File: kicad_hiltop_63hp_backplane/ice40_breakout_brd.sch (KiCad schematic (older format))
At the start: 21 parts, among them J9 SO-DIMM

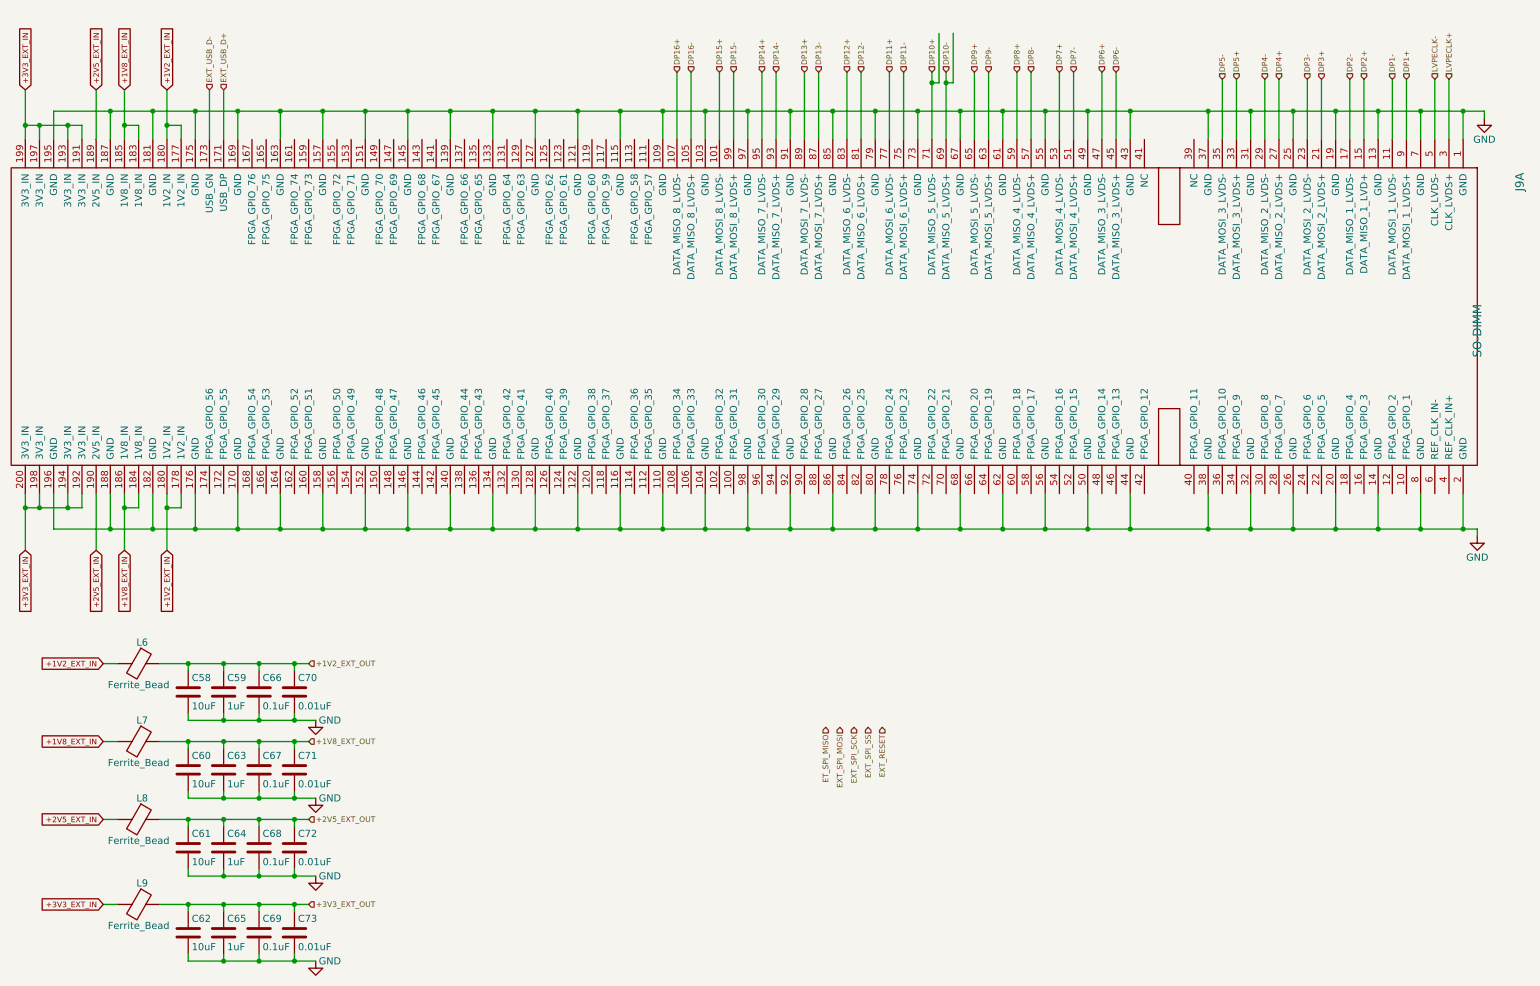
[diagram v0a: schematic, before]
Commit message: root - added pins for SODIMM, added PCI 96 pin connector, pin mapping in progress
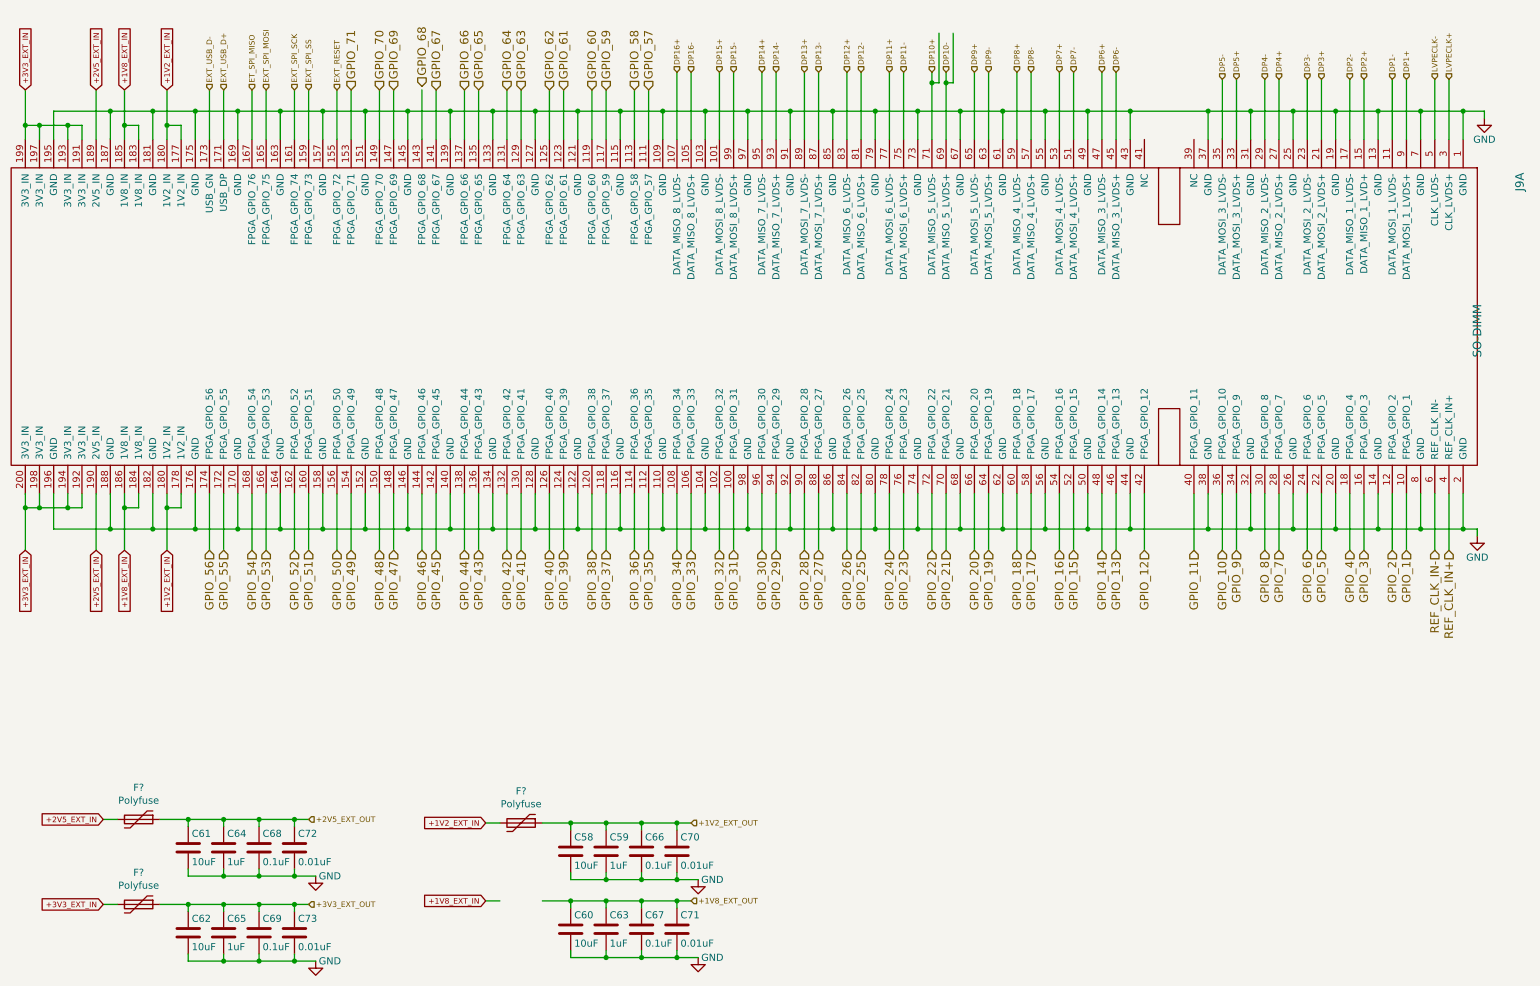
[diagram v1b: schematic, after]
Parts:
- removed L6, L7, L8, L9: Ferrite_Bead, Inductor_SMD:L_0603_1608Metric, symbol device:Ferrite_Bead
- added F? (x3): Polyfuse, symbol device:Polyfuse
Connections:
- net +1V2_EXT_IN: now also F?.2
- net +1V2_EXT_OUT: now also F?.1
- net +2V5_EXT_IN: now also F?.2
- net +2V5_EXT_OUT: now also F?.1
- net +3V3_EXT_IN: now also F?.2
- net +3V3_EXT_OUT: now also F?.1
- net ET_SPI_MISO: now also J9.167 (FPGA_GPIO_76)
- net EXT_RESET: now also J9.155 (FPGA_GPIO_72)
- net EXT_SPI_MOSI: now also J9.165 (FPGA_GPIO_75)
- net EXT_SPI_SCK: now also J9.161 (FPGA_GPIO_74)
- net EXT_SPI_SS: now also J9.159 (FPGA_GPIO_73)
- net GPIO_1: now reaches J9.10 (FPGA_GPIO_1)
- net GPIO_31: now reaches J9.100 (FPGA_GPIO_31)
- net GPIO_32: now reaches J9.102 (FPGA_GPIO_32)
- net GPIO_33: now reaches J9.106 (FPGA_GPIO_33)
- net GPIO_34: now reaches J9.108 (FPGA_GPIO_34)
- net GPIO_57: now reaches J9.111 (FPGA_GPIO_57)
- net GPIO_35: now reaches J9.112 (FPGA_GPIO_35)
- net GPIO_58: now reaches J9.113 (FPGA_GPIO_58)
- net GPIO_36: now reaches J9.114 (FPGA_GPIO_36)
- net GPIO_59: now reaches J9.117 (FPGA_GPIO_59)
- net GPIO_37: now reaches J9.118 (FPGA_GPIO_37)
- net GPIO_60: now reaches J9.119 (FPGA_GPIO_60)
- net GPIO_2: now reaches J9.12 (FPGA_GPIO_2)
- net GPIO_38: now reaches J9.120 (FPGA_GPIO_38)
- net GPIO_61: now reaches J9.123 (FPGA_GPIO_61)
- net GPIO_39: now reaches J9.124 (FPGA_GPIO_39)
- net GPIO_62: now reaches J9.125 (FPGA_GPIO_62)
- net GPIO_40: now reaches J9.126 (FPGA_GPIO_40)
- net GPIO_63: now reaches J9.129 (FPGA_GPIO_63)
- net GPIO_41: now reaches J9.130 (FPGA_GPIO_41)
- net GPIO_64: now reaches J9.131 (FPGA_GPIO_64)
- net GPIO_42: now reaches J9.132 (FPGA_GPIO_42)
- net GPIO_65: now reaches J9.135 (FPGA_GPIO_65)
- net GPIO_43: now reaches J9.136 (FPGA_GPIO_43)
- net GPIO_66: now reaches J9.137 (FPGA_GPIO_66)
- net GPIO_44: now reaches J9.138 (FPGA_GPIO_44)
- net GPIO_67: now reaches J9.141 (FPGA_GPIO_67)
- net GPIO_45: now reaches J9.142 (FPGA_GPIO_45)
- net GPIO_46: now reaches J9.144 (FPGA_GPIO_46)
- net GPIO_69: now reaches J9.147 (FPGA_GPIO_69)
- net GPIO_47: now reaches J9.148 (FPGA_GPIO_47)
- net GPIO_70: now reaches J9.149 (FPGA_GPIO_70)
- net GPIO_48: now reaches J9.150 (FPGA_GPIO_48)
- net GPIO_71: now reaches J9.153 (FPGA_GPIO_71)
- net GPIO_49: now reaches J9.154 (FPGA_GPIO_49)
- net GPIO_50: now reaches J9.156 (FPGA_GPIO_50)
- net GPIO_3: now reaches J9.16 (FPGA_GPIO_3)
- net GPIO_51: now reaches J9.160 (FPGA_GPIO_51)
- net GPIO_52: now reaches J9.162 (FPGA_GPIO_52)
- net GPIO_53: now reaches J9.166 (FPGA_GPIO_53)
- net GPIO_54: now reaches J9.168 (FPGA_GPIO_54)
- net GPIO_55: now reaches J9.172 (FPGA_GPIO_55)
- net GPIO_56: now reaches J9.174 (FPGA_GPIO_56)
- net GPIO_4: now reaches J9.18 (FPGA_GPIO_4)
- net GPIO_5: now reaches J9.22 (FPGA_GPIO_5)
- net GPIO_6: now reaches J9.24 (FPGA_GPIO_6)
- net GPIO_7: now reaches J9.28 (FPGA_GPIO_7)
- net GPIO_8: now reaches J9.30 (FPGA_GPIO_8)
- net GPIO_9: now reaches J9.34 (FPGA_GPIO_9)
- net GPIO_10: now reaches J9.36 (FPGA_GPIO_10)
- net REF_CLK_IN+: now reaches J9.4 (REF_CLK_IN+)
- net GPIO_11: now reaches J9.40 (FPGA_GPIO_11)
- net GPIO_12: now reaches J9.42 (FPGA_GPIO_12)
- net GPIO_13: now reaches J9.46 (FPGA_GPIO_13)
- net GPIO_14: now reaches J9.48 (FPGA_GPIO_14)
- net GPIO_15: now reaches J9.52 (FPGA_GPIO_15)
- net GPIO_16: now reaches J9.54 (FPGA_GPIO_16)
- net GPIO_17: now reaches J9.58 (FPGA_GPIO_17)
- net REF_CLK_IN-: now reaches J9.6 (REF_CLK_IN-)
- net GPIO_18: now reaches J9.60 (FPGA_GPIO_18)
- net GPIO_19: now reaches J9.64 (FPGA_GPIO_19)
- net GPIO_20: now reaches J9.66 (FPGA_GPIO_20)
- net GPIO_21: now reaches J9.70 (FPGA_GPIO_21)
- net GPIO_22: now reaches J9.72 (FPGA_GPIO_22)
- net GPIO_23: now reaches J9.76 (FPGA_GPIO_23)
- net GPIO_24: now reaches J9.78 (FPGA_GPIO_24)
- net GPIO_25: now reaches J9.82 (FPGA_GPIO_25)
- net GPIO_26: now reaches J9.84 (FPGA_GPIO_26)
- net GPIO_27: now reaches J9.88 (FPGA_GPIO_27)
- net GPIO_28: now reaches J9.90 (FPGA_GPIO_28)
- net GPIO_29: now reaches J9.94 (FPGA_GPIO_29)
- net GPIO_30: now reaches J9.96 (FPGA_GPIO_30)
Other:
- moved on the sheet: C58, C59, C60, C63, C66, C67, C70, C71

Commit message: PCI EXPRESS 96
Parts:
- gave numbers to parts that had none: 3
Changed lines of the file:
@@
 GPIO_71
 $Comp
-L device:Polyfuse F?
+L device:Polyfuse F9
 U 1 1 5CEC5F97
 P 1600 6500
-F 0 "F?" V 1375 6500 50  0000 C CNN
+F 0 "F9" V 1375 6500 50  0000 C CNN
 F 1 "Polyfuse" V 1466 6500 50  0000 C CNN
 F 2 "" H 1650 6300 50  0001 L CNN
@@
 $EndComp
 $Comp
-L device:Polyfuse F?
+L device:Polyfuse F10
 U 1 1 5CEC61F6
 P 1600 7100
-F 0 "F?" V 1375 7100 50  0000 C CNN
+F 0 "F10" V 1375 7100 50  0000 C CNN
 F 1 "Polyfuse" V 1466 7100 50  0000 C CNN
 F 2 "" H 1650 6900 50  0001 L CNN
@@
 $EndComp
 $Comp
-L device:Polyfuse F?
+L device:Polyfuse F11
 U 1 1 5CEC625C
 P 4300 6525
-F 0 "F?" V 4075 6525 50  0000 C CNN
+F 0 "F11" V 4075 6525 50  0000 C CNN
 F 1 "Polyfuse" V 4166 6525 50  0000 C CNN
 F 2 "" H 4350 6325 50  0001 L CNN

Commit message: Added new PCB outline for the backplane
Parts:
- C58, C59, C60, C61, C62, C63, C64, C65, C66, C67, C68, C69, C70, C71, C72, C73: symbol device:C -> hiltop_backplane_brd-rescue:C-device
- F10, F11, F9: symbol device:Polyfuse -> hiltop_backplane_brd-rescue:Polyfuse-device
- J9: symbol gti_Lattice:SO-DIMM -> hiltop_backplane_brd-rescue:SO-DIMM-gti_Lattice
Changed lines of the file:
@@
 $EndDescr
 $Comp
-L device:C C58
+L hiltop_backplane_brd-rescue:C-device C58
 U 1 1 5A418459
 P 4650 6725
@@
 $EndComp
 $Comp
-L device:C C59
+L hiltop_backplane_brd-rescue:C-device C59
 U 1 1 5A4184EA
 P 4900 6725
@@
 $EndComp
 $Comp
-L device:C C66
+L hiltop_backplane_brd-rescue:C-device C66
 U 1 1 5A41850F
 P 5150 6725
@@
 $EndComp
 $Comp
-L device:C C70
+L hiltop_backplane_brd-rescue:C-device C70
 U 1 1 5A418541
 P 5400 6725
@@
 $EndComp
 $Comp
-L device:C C60
+L hiltop_backplane_brd-rescue:C-device C60
 U 1 1 5A41856A
 P 4650 7275
@@
 $EndComp
 $Comp
-L device:C C63
+L hiltop_backplane_brd-rescue:C-device C63
 U 1 1 5A4185BC
 P 4900 7275
@@
 $EndComp
 $Comp
-L device:C C67
+L hiltop_backplane_brd-rescue:C-device C67
 U 1 1 5A4185F9
 P 5150 7275
@@
 $EndComp
 $Comp
-L device:C C71
+L hiltop_backplane_brd-rescue:C-device C71
 U 1 1 5A41862F
 P 5400 7275
@@
 $EndComp
 $Comp
-L device:C C61
+L hiltop_backplane_brd-rescue:C-device C61
 U 1 1 5A418664
 P 1950 6700
@@
 $EndComp
 $Comp
-L device:C C64
+L hiltop_backplane_brd-rescue:C-device C64
 U 1 1 5A4186B2
 P 2200 6700
@@
 $EndComp
 $Comp
-L device:C C68
+L hiltop_backplane_brd-rescue:C-device C68
 U 1 1 5A4186E9
 P 2450 6700
@@
 $EndComp
 $Comp
-L device:C C72
+L hiltop_backplane_brd-rescue:C-device C72
 U 1 1 5A418729
 P 2700 6700
@@
 $EndComp
 $Comp
-L device:C C62
+L hiltop_backplane_brd-rescue:C-device C62
 U 1 1 5A418776
 P 1950 7300
@@
 $EndComp
 $Comp
-L device:C C65
+L hiltop_backplane_brd-rescue:C-device C65
 U 1 1 5A418B7E
 P 2200 7300
@@
 $EndComp
 $Comp
-L device:C C69
+L hiltop_backplane_brd-rescue:C-device C69
 U 1 1 5A418BC9
 P 2450 7300
@@
 $EndComp
 $Comp
-L device:C C73
+L hiltop_backplane_brd-rescue:C-device C73
 U 1 1 5A418C13
 P 2700 7300
@@
 	8600 1500 9150 1500
 $Comp
-L gti_Lattice:SO-DIMM J9
+L hiltop_backplane_brd-rescue:SO-DIMM-gti_Lattice J9
 U 1 1 5A3A8985
 P 11200 2950
@@
 GPIO_71
 $Comp
-L device:Polyfuse F9
+L hiltop_backplane_brd-rescue:Polyfuse-device F9
 U 1 1 5CEC5F97
 P 1600 6500
@@
 $EndComp
 $Comp
-L device:Polyfuse F10
+L hiltop_backplane_brd-rescue:Polyfuse-device F10
 U 1 1 5CEC61F6
 P 1600 7100
@@
 $EndComp
 $Comp
-L device:Polyfuse F11
+L hiltop_backplane_brd-rescue:Polyfuse-device F11
 U 1 1 5CEC625C
 P 4300 6525
